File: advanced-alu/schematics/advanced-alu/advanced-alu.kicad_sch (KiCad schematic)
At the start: 3 parts

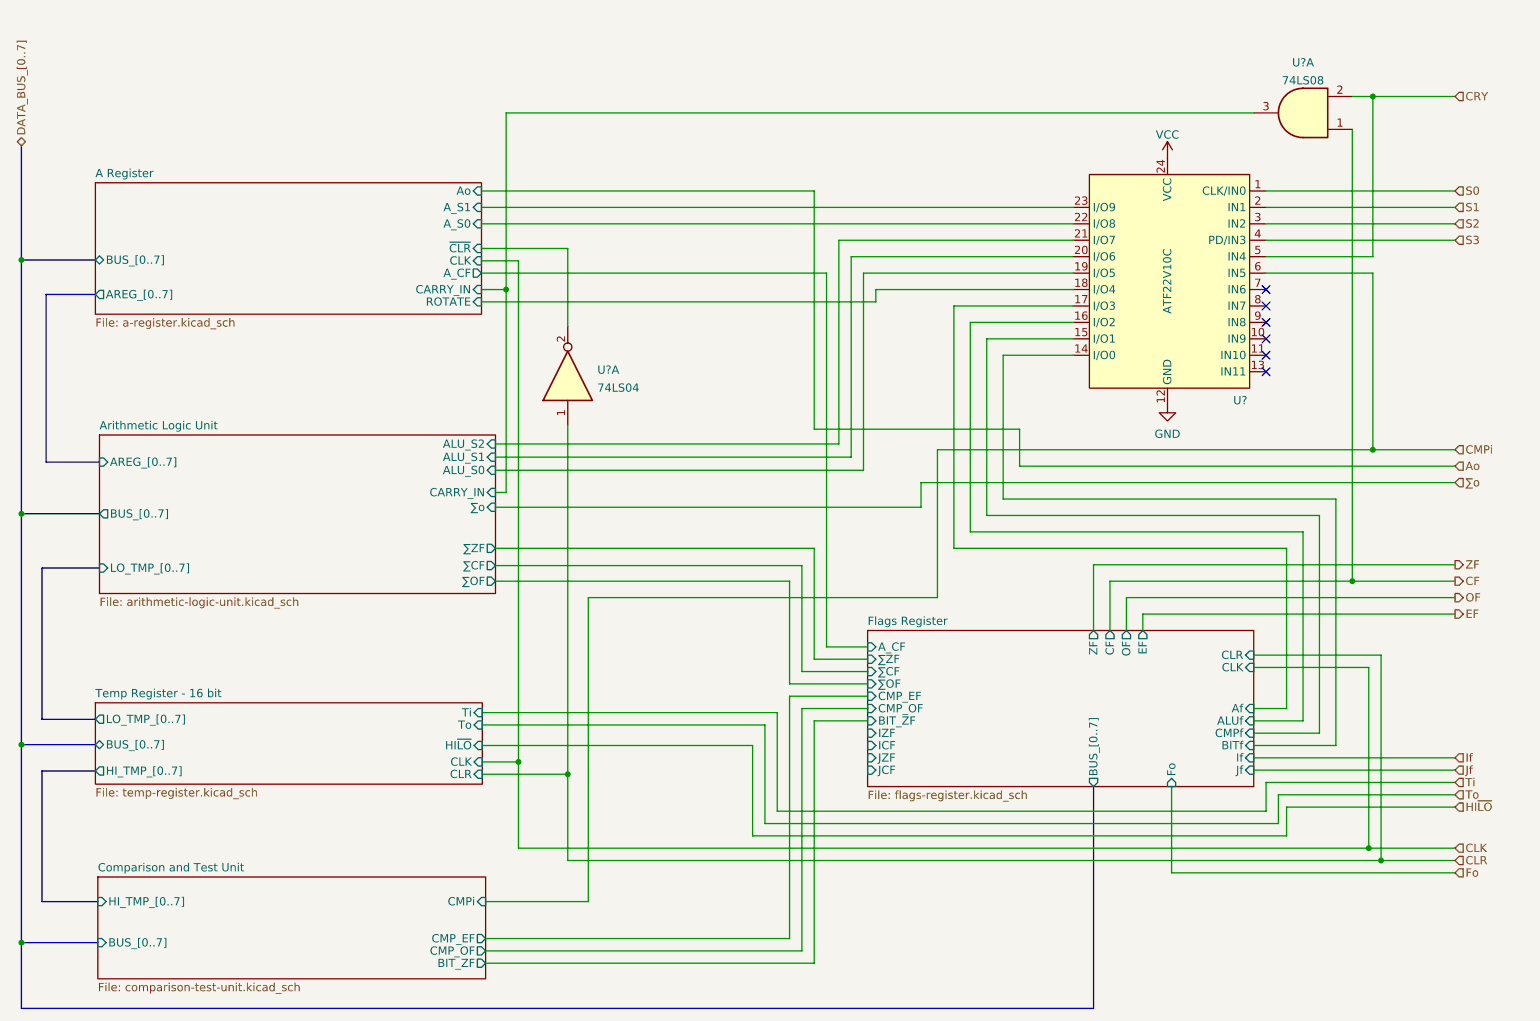
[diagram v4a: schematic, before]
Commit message: updated flags register
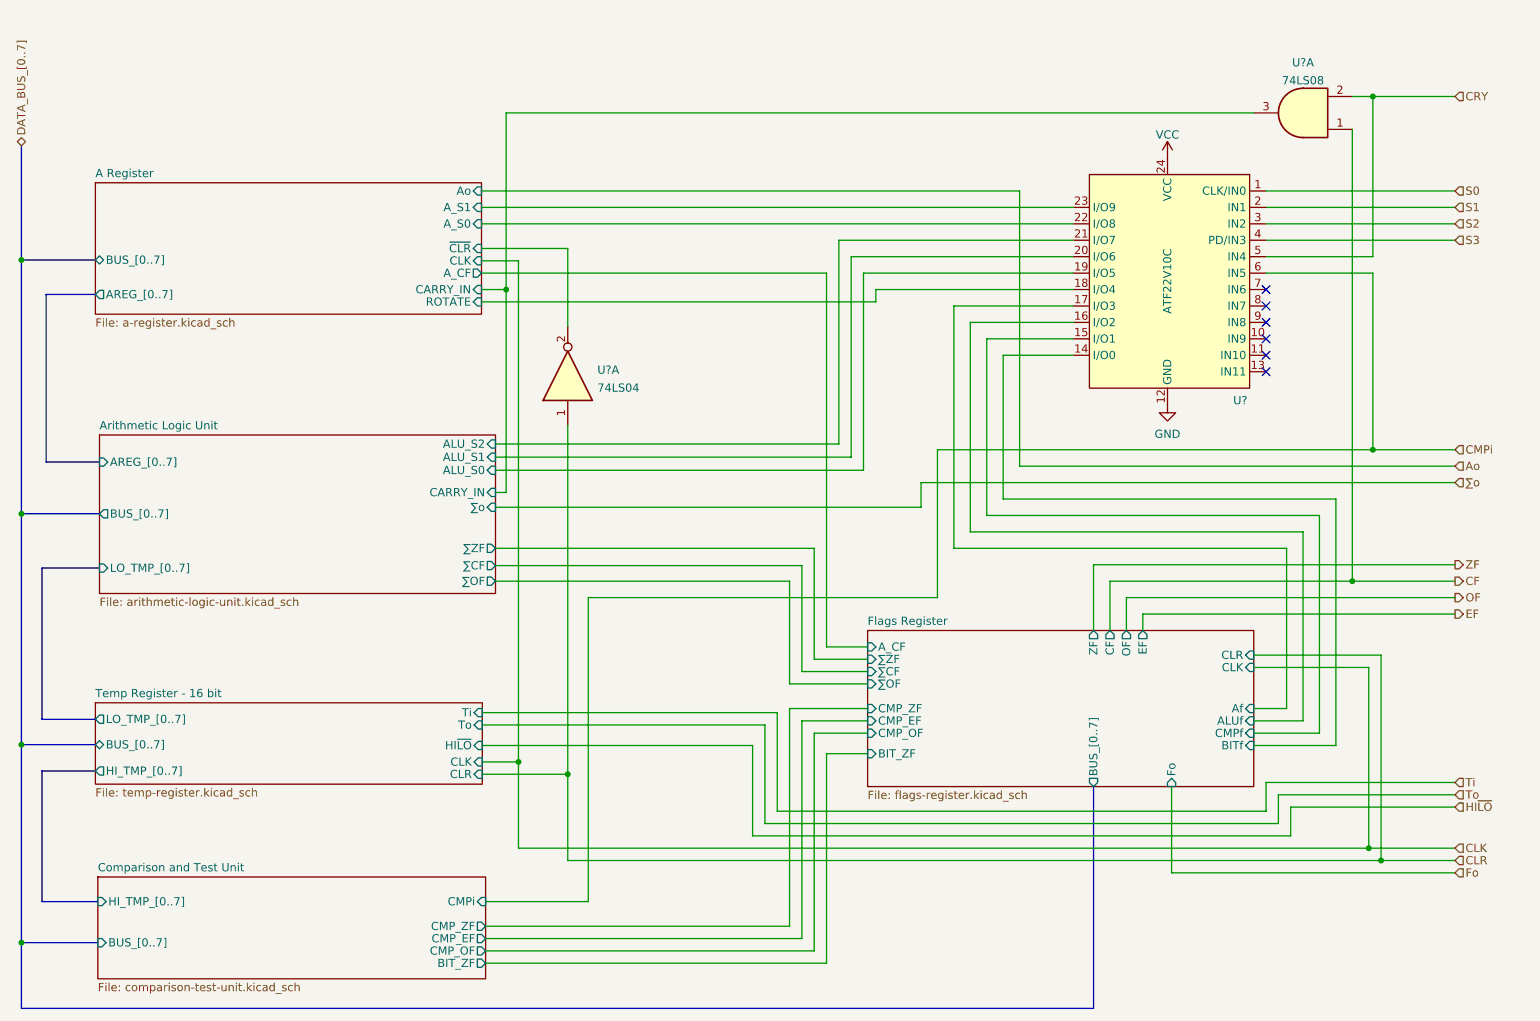
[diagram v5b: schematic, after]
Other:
- sheet Comparison and Test Unit ports: added CMP_ZF; removed none
- sheet Flags Register ports: added CMP_ZF; removed ICF, IZF, If, JCF, JZF, Jf
